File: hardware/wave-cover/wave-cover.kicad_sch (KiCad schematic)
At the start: 11 parts

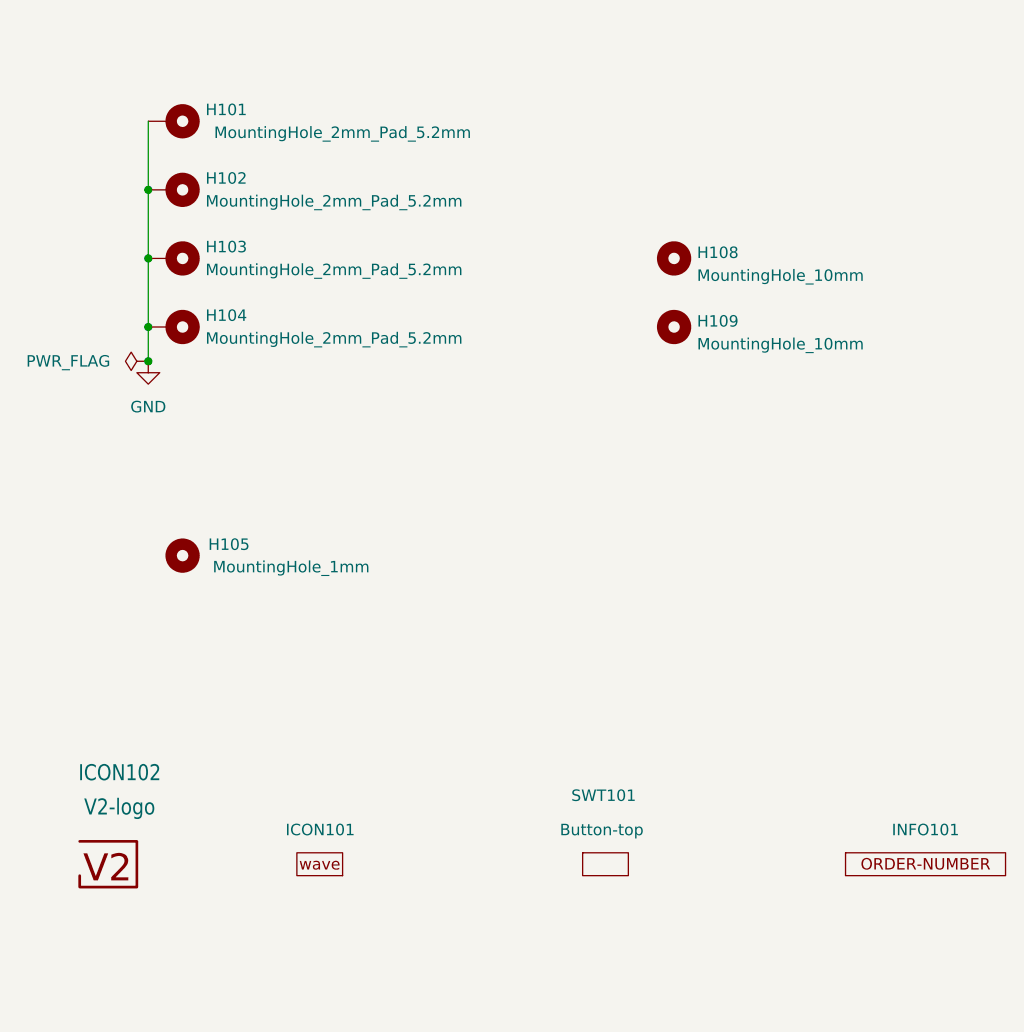
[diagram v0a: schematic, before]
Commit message: Replace Order_Number
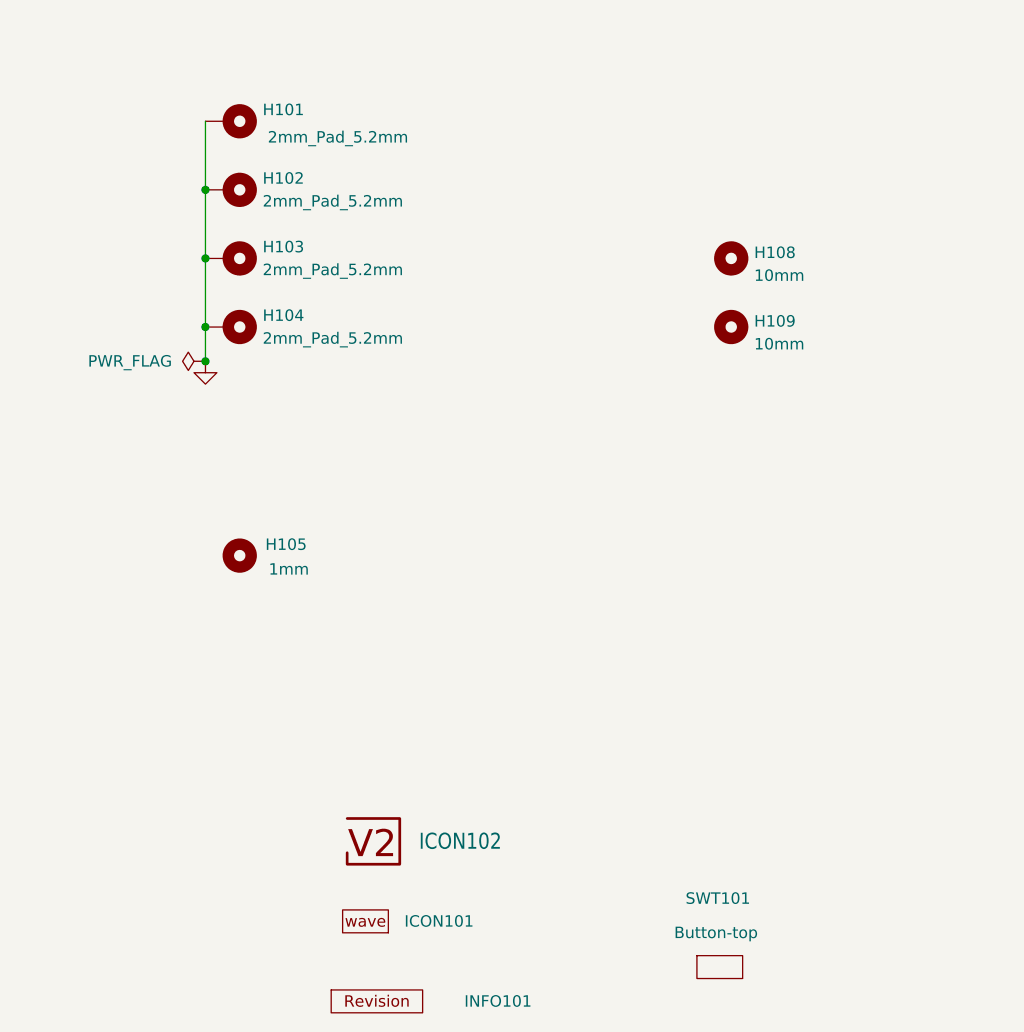
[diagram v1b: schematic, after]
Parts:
- H101, H102, H103, H104: value MountingHole_2mm_Pad_5.2mm -> 2mm_Pad_5.2mm; footprint V2_Mechanical:Mounting_Hole_2mm_Pad_5.2mm -> V2_Mechanical:MountingHole_2mm_Pad_5.2mm
- H105: value MountingHole_1mm -> 1mm
- H108, H109: value MountingHole_10mm -> 10mm
- INFO101: value ORDER-NUMBER -> ~; footprint V2_Production:Order_Number -> V2_Production:Revision; symbol V2_Production:Order_Number -> V2_Production:Revision
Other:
- moved on the sheet: H101, H102, H103, H104, H105, H108, H109, ICON101, ICON102, INFO101, SWT101

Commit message: Update Library
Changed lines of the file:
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@@
-	)
-	(junction
-		(at 111.76 85.09)
-		(diameter 0)
-		(color 0 0 0 0)
 	)
 	(junction
@@
 		(dnp no)
 		(fields_autoplaced yes)
-		(property "Reference" "#PWR0101"
+		(property "Reference" "#PWR101"
 			(at 111.76 91.44 0)
 			(effects
@@
 			(project "wave-cover"
 				(path "/6c8448b4-b04d-47e1-934e-e40cbe27a7be"
-					(reference "#PWR0101")
+					(reference "#PWR101")
 					(unit 1)
 				)
@@
 	)
 	(symbol
+		(lib_id "V2_power:GND")
+		(at 123.19 48.26 90)
+		(unit 1)
+		(exclude_from_sim no)
+		(in_bom yes)
+		(on_board yes)
+		(dnp no)
+		(fields_autoplaced yes)
+		(property "Reference" "#PWR0102"
+			(at 129.54 48.26 0)
+			(effects
+				(font
+					(size 1.27 1.27)
+				)
+				(hide yes)
+			)
+		)
+		(property "Value" "GND"
+			(at 128.27 48.26 0)
+			(effects
+				(font
+					(size 1.27 1.27)
+				)
+				(hide yes)
+			)
+		)
+		(property "Footprint" ""
+			(at 123.19 48.26 0)
+			(effects
+				(font
+					(size 1.27 1.27)
+				)
+				(hide yes)
+			)
+		)
+		(property "Datasheet" ""
+			(at 123.19 48.26 0)
+			(effects
+				(font
+					(size 1.27 1.27)
+				)
+				(hide yes)
+			)
+		)
+		(property "Description" ""
+			(at 123.19 48.26 0)
+			(effects
+				(font
+					(size 1.27 1.27)
+				)
+				(hide yes)
+			)
+		)
+		(pin "1"
+		)
+		(instances
+			(project "wave-cover"
+				(path "/6c8448b4-b04d-47e1-934e-e40cbe27a7be"
+					(reference "#PWR0102")
+					(unit 1)
+				)
+			)
+		)
+	)
+	(symbol
+		(lib_id "V2_power:PWR_FLAG")
+		(at 123.19 48.26 0)
+		(unit 1)
+		(exclude_from_sim no)
+		(in_bom yes)
+		(on_board yes)
+		(dnp no)
+		(property "Reference" "#FLG0102"
+			(at 123.19 46.355 0)
+			(effects
+				(font
+					(size 1.27 1.27)
+				)
+				(hide yes)
+			)
+		)
+		(property "Value" "PWR_FLAG"
+			(at 114.808 48.26 0)
+			(effects
+				(font
+					(size 1.27 1.27)
+				)
+			)
+		)
+		(property "Footprint" ""
+			(at 123.19 48.26 0)
+			(effects
+				(font
+					(size 1.27 1.27)
+				)
+				(hide yes)
+			)
+		)
+		(property "Datasheet" ""
+			(at 123.19 48.26 0)
+			(effects
+				(font
+					(size 1.27 1.27)
+				)
+				(hide yes)
+			)
+		)
+		(property "Description" "Special symbol for telling ERC where power comes from"
+			(at 123.19 48.26 0)
+			(effects
+				(font
+					(size 1.27 1.27)
+				)
+				(hide yes)
+			)
+		)
+		(pin "1"
+		)
+		(instances
+			(project "wave-cover"
+				(path "/6c8448b4-b04d-47e1-934e-e40cbe27a7be"
+					(reference "#FLG0102")
+					(unit 1)
+				)
+			)
+		)
+	)
+	(symbol
 		(lib_id "V2_Artwork:Board_wave")
 		(at 129.54 147.32 0)
@@
 					(unit 1)
 				)
-			)
-		)
-	)
-	(symbol
-		(lib_id "V2_power:PWR_FLAG")
-		(at 111.76 85.09 0)
-		(unit 1)
-		(exclude_from_sim no)
-		(in_bom yes)
-		(on_board yes)
-		(dnp no)
-		(property "Reference" "#FLG0101"
-			(at 111.76 83.185 0)
-			(effects
-				(font
-					(size 1.27 1.27)
-				)
-				(hide yes)
-			)
-		)
-		(property "Value" "PWR_FLAG"
-			(at 103.378 85.09 0)
-			(effects
-				(font
-					(size 1.27 1.27)
-				)
-			)
-		)
-		(property "Footprint" ""
-			(at 111.76 85.09 0)
-			(effects
-				(font
-					(size 1.27 1.27)
-				)
-				(hide yes)
-			)
-		)
-		(property "Datasheet" ""
-			(at 111.76 85.09 0)
-			(effects
-				(font
-					(size 1.27 1.27)
-				)
-				(hide yes)
-			)
-		)
-		(property "Description" "Special symbol for telling ERC where power comes from"
-			(at 111.76 85.09 0)
-			(effects
-				(font
-					(size 1.27 1.27)
-				)
-				(hide yes)
-			)
-		)
-		(pin "1"
-		)
-		(instances
-			(project "wave-cover"
-				(path "/6c8448b4-b04d-47e1-934e-e40cbe27a7be"
-					(reference "#FLG0101")
-					(unit 1)
-				)
